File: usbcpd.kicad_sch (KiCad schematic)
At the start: 31 parts, among them J1 USB_C_Receptacle_USB2.0_14P, J3 USB_C_Receptacle_USB2.0, U4 STUSB4500QTR, U5 VBA4658, U6 STUSB4500QTR, U7 VBA4658

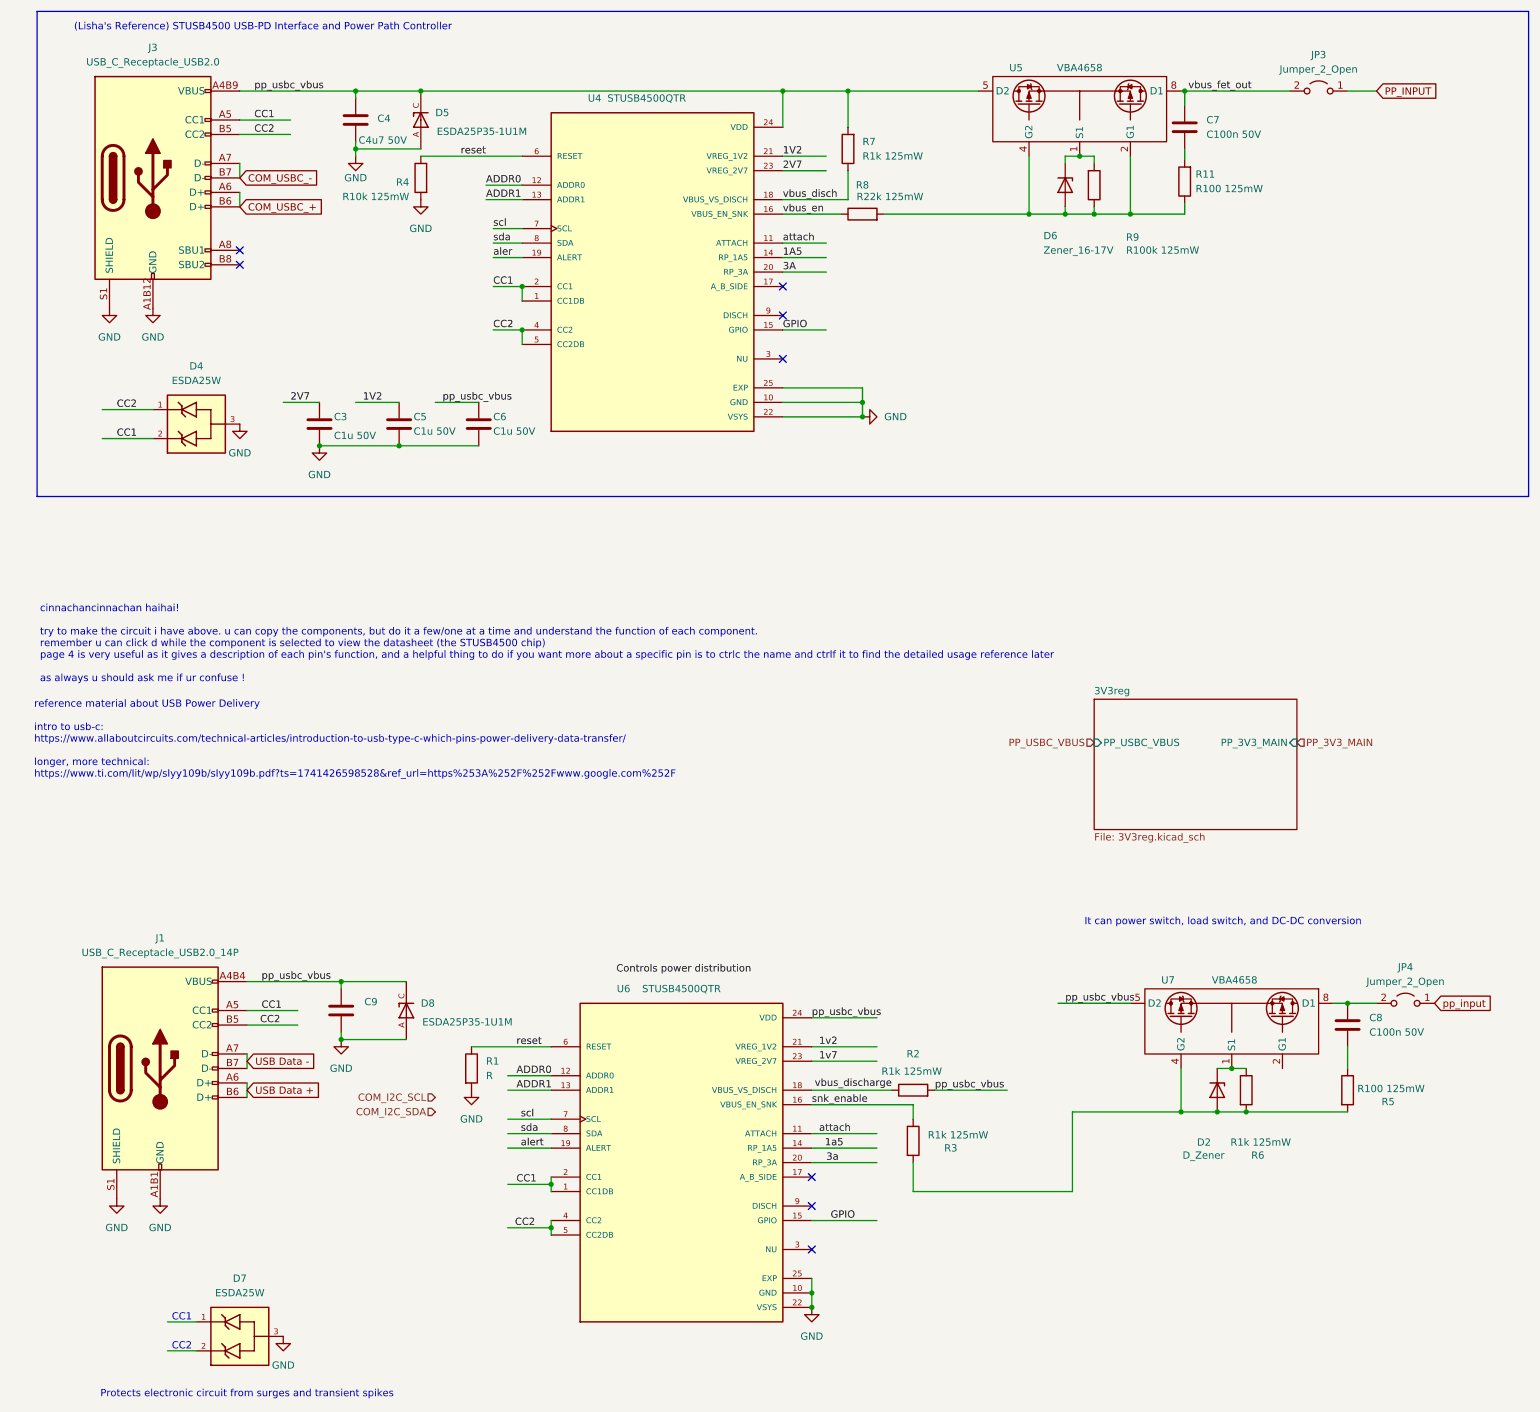
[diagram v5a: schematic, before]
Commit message: Cleanup, add 5vREG block
Signed-off-by: sanyue <sanyue7th@gmail.com>
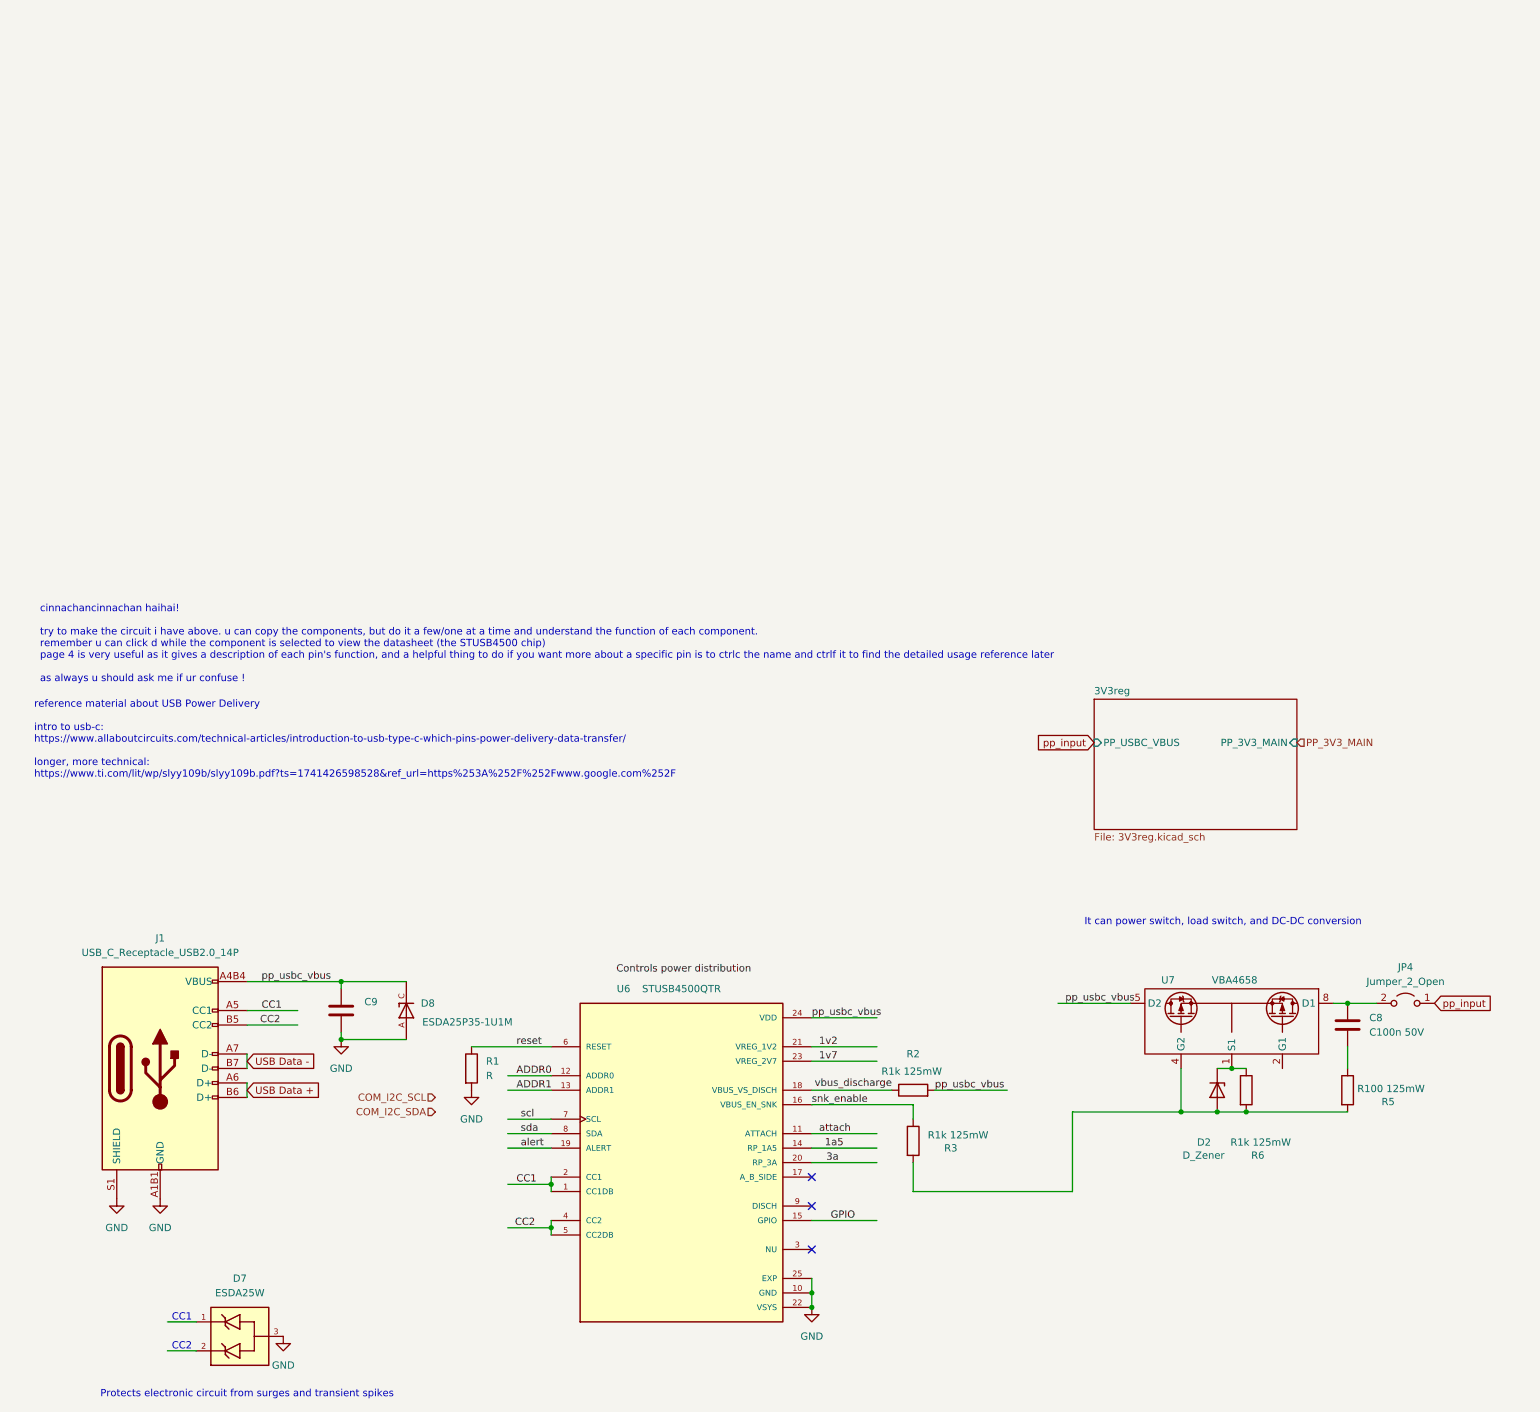
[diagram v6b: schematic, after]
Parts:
- removed C3, C5, C6: C1u 50V, Capacitor_SMD:C_0402_1005Metric, symbol Device:C
- removed C4: C4u7 50V, Capacitor_SMD:C_0603_1608Metric, symbol Device:C
- removed C7: C100n 50V, Capacitor_SMD:C_0402_1005Metric, symbol Device:C
- removed D4: ESDA25W, SOT65P210X110-3N, symbol aaafootprintlib:ESDA25W
- removed D5: ESDA25P35-1U1M, TVS_ESDA25P35-1U1M, symbol aaafootprintlib:ESDA25P35-1U1M
- removed D6: Zener_16-17V, Diode_SMD:D_SOD-123, symbol Device:D_Zener
- removed J3: USB_C_Receptacle_USB2.0, MC-110LD [USB-C], symbol Connector:USB_C_Receptacle_USB2.0
- removed JP3: Jumper_2_Open, Jumper:SolderJumper-2_P1.3mm_Open_TrianglePad1.0x1.5mm, symbol Jumper:Jumper_2_Open
- removed R11: R100 125mW, Resistor_SMD:R_0402_1005Metric, symbol Device:R
- removed R4: R10k 125mW, Resistor_SMD:R_0402_1005Metric, symbol Device:R
- removed R7: R1k 125mW, Resistor_SMD:R_0402_1005Metric, symbol Device:R
- removed R8: R22k 125mW, Resistor_SMD:R_0402_1005Metric, symbol Device:R
- removed R9: R100k 125mW, Resistor_SMD:R_0402_1005Metric, symbol Device:R
- removed U4: STUSB4500QTR, QFN50P400X400X100-25N, symbol aaafootprintlib:STUSB4500LQTR
- removed U5: VBA4658, Package_SO:SO-8_3.9x4.9mm_P1.27mm, symbol aaafootprintlib:VBA4658
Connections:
- no-connect marks 8 -> 3
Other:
- note removed: "(Lisha's Reference) STUSB4500 USB-PD Interface and Power Path Controller"

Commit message: layout
Signed-off-by: sanyue <sanyue7th@gmail.com>
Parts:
- D7: footprint SOT65P210X110-3N -> aaafootprintlib:SOT65P210X110-3N
- D8: footprint TVS_ESDA25P35-1U1M -> aaafootprintlib:TVS_ESDA25P35-1U1M
- J1: footprint (none) -> Connector_USB:USB_C_Receptacle_GCT_USB4105-xx-A_16P_TopMnt_Horizontal
- U6: footprint QFN50P400X400X100-25N -> aaafootprintlib:QFN50P400X400X100-25N
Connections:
- net scl is gone; now on net COM_I2C_SCL: U6.7 (SCL)
- net sda is gone; now on net COM_I2C_SDA: U6.8 (SDA)
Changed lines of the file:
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@@
 	(hierarchical_label "COM_I2C_SCL"
 		(shape input)
-		(at 83.82 102.87 180)
+		(at 96.52 106.68 180)
 		(effects
 			(font
@@
 	(hierarchical_label "COM_I2C_SDA"
 		(shape input)
-		(at 83.82 105.41 180)
+		(at 96.52 109.22 180)
 		(effects
 			(font
@@
 			)
 		)
+		(property "Sim.Device" ""
+			(at 254 86.36 0)
+			(effects
+				(font
+					(size 1.27 1.27)
+				)
+			)
+		)
+		(property "Sim.Pins" ""
+			(at 254 86.36 0)
+			(effects
+				(font
+					(size 1.27 1.27)
+				)
+			)
+		)
 		(pin "1"
 		)
@@
 			)
 		)
-		(property "Footprint" "SOT65P210X110-3N"
+		(property "Footprint" "aaafootprintlib:SOT65P210X110-3N"
 			(at 49.53 144.78 0)
 			(effects
@@
 				)
 				(hide yes)
+			)
+		)
+		(property "Sim.Device" ""
+			(at 49.53 144.78 0)
+			(effects
+				(font
+					(size 1.27 1.27)
+				)
+			)
+		)
+		(property "Sim.Pins" ""
+			(at 49.53 144.78 0)
+			(effects
+				(font
+					(size 1.27 1.27)
+				)
 			)
 		)
@@
 			)
 		)
+		(property "Sim.Device" ""
+			(at 243.84 90.17 0)
+			(effects
+				(font
+					(size 1.27 1.27)
+				)
+			)
+		)
+		(property "Sim.Pins" ""
+			(at 243.84 90.17 0)
+			(effects
+				(font
+					(size 1.27 1.27)
+				)
+			)
+		)
 		(pin "2"
 		)
@@
 			)
 		)
-		(property "Footprint" ""
+		(property "Footprint" "Connector_USB:USB_C_Receptacle_GCT_USB4105-xx-A_16P_TopMnt_Horizontal"
 			(at 39.37 97.79 0)
 			(effects
@@
 				)
 				(hide yes)
+			)
+		)
+		(property "Sim.Device" ""
+			(at 35.56 97.79 0)
+			(effects
+				(font
+					(size 1.27 1.27)
+				)
+			)
+		)
+		(property "Sim.Pins" ""
+			(at 35.56 97.79 0)
+			(effects
+				(font
+					(size 1.27 1.27)
+				)
 			)
 		)
@@
 			)
 		)
+		(property "Sim.Device" ""
+			(at 224.79 80.01 0)
+			(effects
+				(font
+					(size 1.27 1.27)
+				)
+			)
+		)
+		(property "Sim.Pins" ""
+			(at 224.79 80.01 0)
+			(effects
+				(font
+					(size 1.27 1.27)
+				)
+			)
+		)
 		(pin "1"
 		)
@@
 			)
 		)
+		(property "Sim.Device" ""
+			(at 67.31 87.63 0)
+			(effects
+				(font
+					(size 1.27 1.27)
+				)
+			)
+		)
+		(property "Sim.Pins" ""
+			(at 67.31 87.63 0)
+			(effects
+				(font
+					(size 1.27 1.27)
+				)
+			)
+		)
 		(pin "2"
 		)
@@
 				)
 				(hide yes)
+			)
+		)
+		(property "Sim.Device" ""
+			(at 167.64 110.49 0)
+			(effects
+				(font
+					(size 1.27 1.27)
+				)
+			)
+		)
+		(property "Sim.Pins" ""
+			(at 167.64 110.49 0)
+			(effects
+				(font
+					(size 1.27 1.27)
+				)
 			)
 		)
@@
 			)
 		)
+		(property "Sim.Device" ""
+			(at 226.06 101.6 0)
+			(effects
+				(font
+					(size 1.27 1.27)
+				)
+			)
+		)
+		(property "Sim.Pins" ""
+			(at 226.06 101.6 0)
+			(effects
+				(font
+					(size 1.27 1.27)
+				)
+			)
+		)
 		(pin "1"
 		)
@@
 			)
 		)
+		(property "Sim.Device" ""
+			(at 90.17 97.79 0)
+			(effects
+				(font
+					(size 1.27 1.27)
+				)
+			)
+		)
+		(property "Sim.Pins" ""
+			(at 90.17 97.79 0)
+			(effects
+				(font
+					(size 1.27 1.27)
+				)
+			)
+		)
 		(pin "2"
 		)
@@
 			)
 		)
-		(property "Footprint" "TVS_ESDA25P35-1U1M"
+		(property "Footprint" "aaafootprintlib:TVS_ESDA25P35-1U1M"
 			(at 78.74 87.63 0)
 			(effects
@@
 			)
 		)
+		(property "Sim.Device" ""
+			(at 78.74 87.63 0)
+			(effects
+				(font
+					(size 1.27 1.27)
+				)
+			)
+		)
+		(property "Sim.Pins" ""
+			(at 78.74 87.63 0)
+			(effects
+				(font
+					(size 1.27 1.27)
+				)
+			)
+		)
 		(pin "C"
 		)
@@
 			)
 		)
+		(property "Sim.Device" ""
+			(at 220.98 101.6 0)
+			(effects
+				(font
+					(size 1.27 1.27)
+				)
+			)
+		)
+		(property "Sim.Pins" ""
+			(at 220.98 101.6 0)
+			(effects
+				(font
+					(size 1.27 1.27)
+				)
+			)
+		)
 		(pin "1"
 		)
@@
 			)
 		)
+		(property "Sim.Device" ""
+			(at 243.84 101.6 0)
+			(effects
+				(font
+					(size 1.27 1.27)
+				)
+			)
+		)
+		(property "Sim.Pins" ""
+			(at 243.84 101.6 0)
+			(effects
+				(font
+					(size 1.27 1.27)
+				)
+			)
+		)
 		(pin "1"
 		)
@@
 				)
 				(hide yes)
+			)
+		)
+		(property "Sim.Device" ""
+			(at 167.64 101.6 0)
+			(effects
+				(font
+					(size 1.27 1.27)
+				)
+			)
+		)
+		(property "Sim.Pins" ""
+			(at 167.64 101.6 0)
+			(effects
+				(font
+					(size 1.27 1.27)
+				)
 			)
 		)
@@
 			)
 		)
-		(property "Footprint" "QFN50P400X400X100-25N"
+		(property "Footprint" "aaafootprintlib:QFN50P400X400X100-25N"
 			(at 127 114.3 0)
 			(effects
@@
 			)
 		)
+		(property "Sim.Device" ""
+			(at 127 114.3 0)
+			(effects
+				(font
+					(size 1.27 1.27)
+				)
+			)
+		)
+		(property "Sim.Pins" ""
+			(at 127 114.3 0)
+			(effects
+				(font
+					(size 1.27 1.27)
+				)
+			)
+		)
